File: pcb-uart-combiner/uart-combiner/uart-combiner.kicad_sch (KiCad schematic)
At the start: 26 parts, among them J1 Conn_01x03, J5 DBG UART, J6 SWD, J7 Conn_01x03, J8 Conn_01x03, J9 Conn_01x03

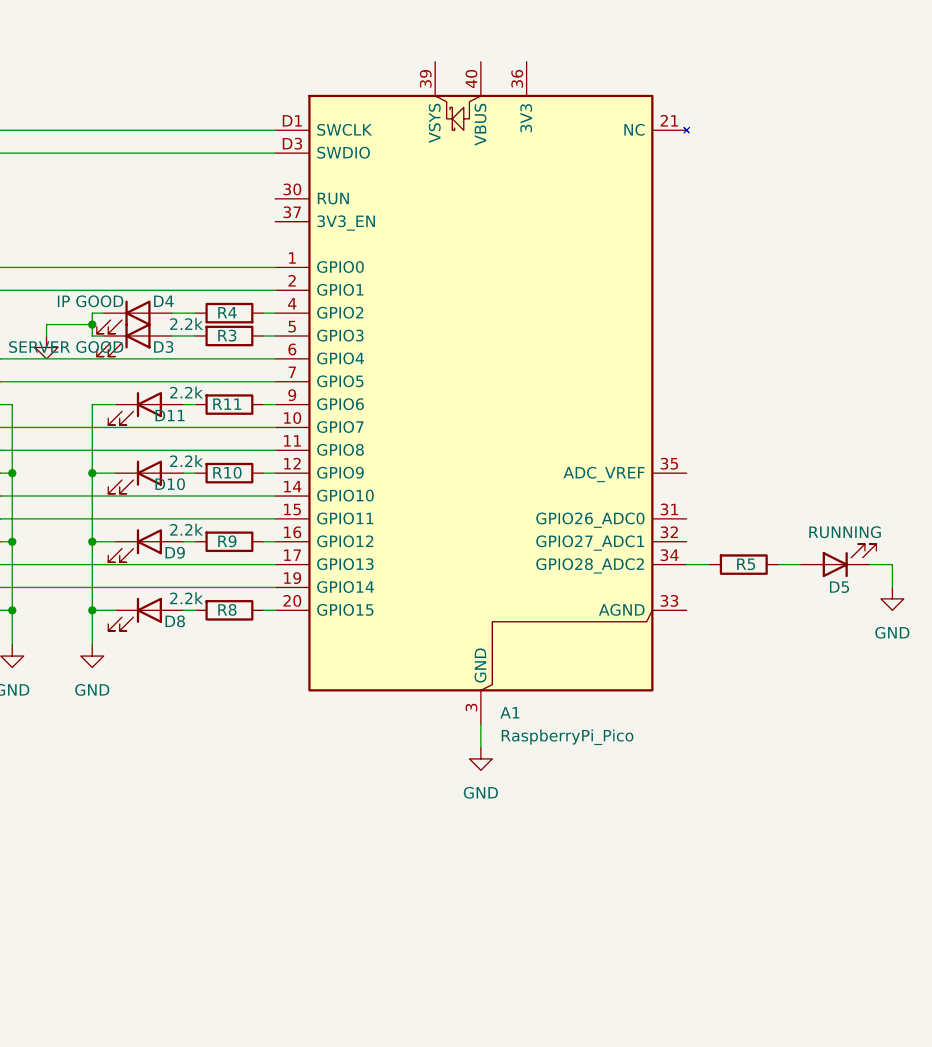
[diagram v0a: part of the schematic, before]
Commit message: Adjusting board size.
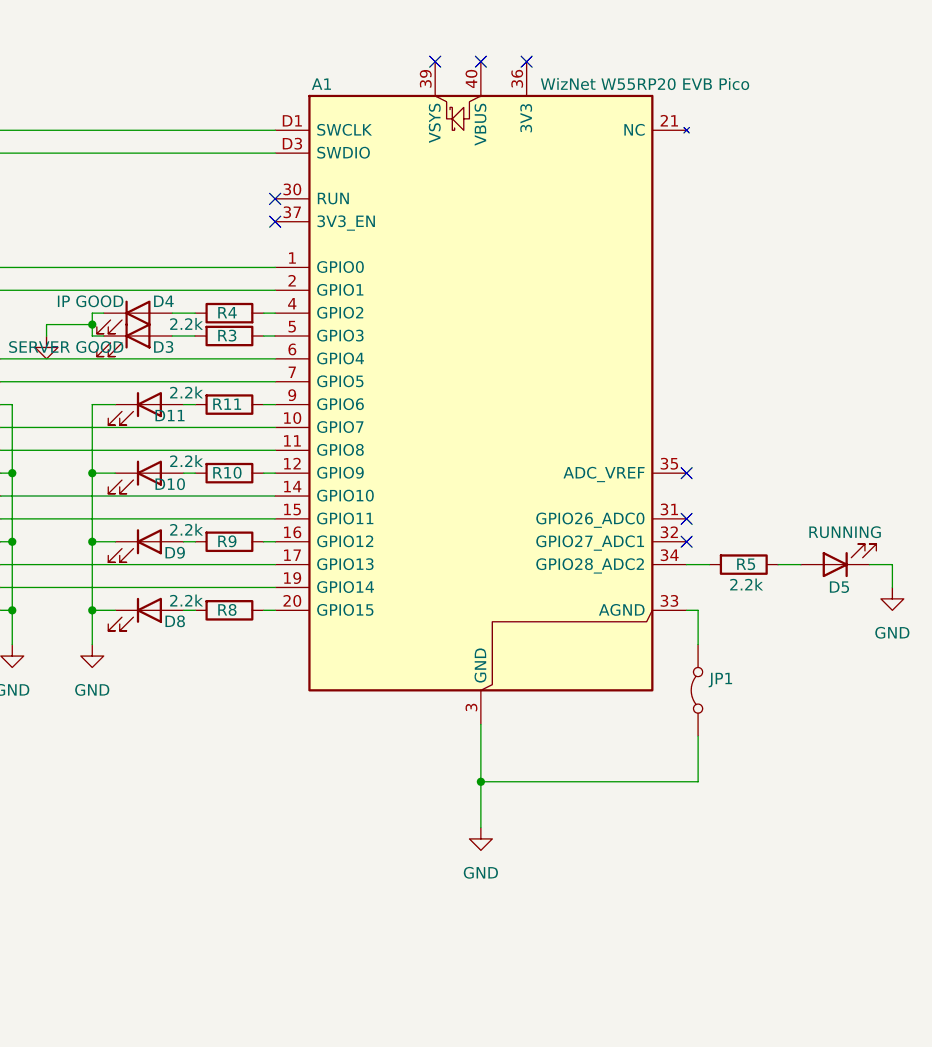
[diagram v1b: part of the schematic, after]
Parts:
- added JP1: Jumper_2_Bridged, Jumper:SolderJumper-2_P1.3mm_Bridged_RoundedPad1.0x1.5mm, symbol Jumper:Jumper_2_Bridged
- A1: value RaspberryPi_Pico -> WizNet W55RP20 EVB Pico
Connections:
- net GND: now also JP1.1 (A)
- net at A1.33 (AGND): now also JP1.2 (B)
- no-connect marks 0 -> 8
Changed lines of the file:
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@@
 	)
 	(junction
+		(at 114.3 130.81)
+		(diameter 0)
+		(color 0 0 0 0)
+	)
+	(junction
 		(at 71.12 80.01)
 		(diameter 0)
@@
 		(color 0 0 0 0)
 	)
+	(no_connect
+		(at 114.3 50.8)
+	)
+	(no_connect
+		(at 119.38 50.8)
+	)
+	(no_connect
+		(at 109.22 50.8)
+	)
+	(no_connect
+		(at 137.16 101.6)
+	)
+	(no_connect
+		(at 137.16 104.14)
+	)
+	(no_connect
+		(at 137.16 96.52)
+	)
+	(no_connect
+		(at 91.44 66.04)
+	)
+	(no_connect
+		(at 91.44 68.58)
+	)
 	(wire
 		(pts
@@
 	(wire
 		(pts
-			(xy 114.3 124.46) (xy 114.3 127)
+			(xy 114.3 124.46) (xy 114.3 130.81)
 		)
 		(stroke
@@
 	(wire
 		(pts
+			(xy 138.43 111.76) (xy 138.43 115.57)
+		)
+		(stroke
+			(width 0)
+			(type default)
+		)
+	)
+	(wire
+		(pts
 			(xy 90.17 78.74) (xy 91.44 78.74)
 		)
@@
 	(wire
 		(pts
+			(xy 138.43 130.81) (xy 114.3 130.81)
+		)
+		(stroke
+			(width 0)
+			(type default)
+		)
+	)
+	(wire
+		(pts
 			(xy 60.96 111.76) (xy 62.23 111.76)
 		)
@@
 	(wire
 		(pts
+			(xy 138.43 125.73) (xy 138.43 130.81)
+		)
+		(stroke
+			(width 0)
+			(type default)
+		)
+	)
+	(wire
+		(pts
 			(xy 60.96 109.22) (xy 91.44 109.22)
 		)
@@
 	(wire
 		(pts
+			(xy 114.3 130.81) (xy 114.3 135.89)
+		)
+		(stroke
+			(width 0)
+			(type default)
+		)
+	)
+	(wire
+		(pts
 			(xy 60.96 104.14) (xy 62.23 104.14)
 		)
@@
 	(wire
 		(pts
+			(xy 137.16 111.76) (xy 138.43 111.76)
+		)
+		(stroke
+			(width 0)
+			(type default)
+		)
+	)
+	(wire
+		(pts
 			(xy 53.34 68.58) (xy 53.34 77.47)
 		)
@@
 	(symbol
 		(lib_id "power:GND")
-		(at 114.3 127 0)
+		(at 114.3 135.89 0)
 		(unit 1)
 		(body_style 1)
@@
 		(fields_autoplaced yes)
 		(property "Reference" "#PWR05"
-			(at 114.3 133.35 0)
+			(at 114.3 142.24 0)
 			(hide yes)
 			(show_name no)
@@
 		)
 		(property "Value" "GND"
-			(at 114.3 132.08 0)
+			(at 114.3 140.97 0)
 			(show_name no)
 			(do_not_autoplace no)
@@
 		)
 		(property "Footprint" ""
-			(at 114.3 127 0)
+			(at 114.3 135.89 0)
 			(hide yes)
 			(show_name no)
@@
 		)
 		(property "Datasheet" ""
-			(at 114.3 127 0)
+			(at 114.3 135.89 0)
 			(hide yes)
 			(show_name no)
@@
 		)
 		(property "Description" "Power symbol creates a global label with name \"GND\" , ground"
-			(at 114.3 127 0)
+			(at 114.3 135.89 0)
 			(hide yes)
 			(show_name no)
@@
 	)
 	(symbol
+		(lib_id "Jumper:Jumper_2_Bridged")
+		(at 138.43 120.65 90)
+		(unit 1)
+		(body_style 1)
+		(exclude_from_sim no)
+		(in_bom yes)
+		(on_board yes)
+		(in_pos_files yes)
+		(dnp no)
+		(fields_autoplaced yes)
+		(property "Reference" "JP1"
+			(at 139.7 119.3799 90)
+			(show_name no)
+			(do_not_autoplace no)
+			(effects
+				(font
+					(size 1.27 1.27)
+				)
+				(justify right)
+			)
+		)
+		(property "Value" "Jumper_2_Bridged"
+			(at 139.7 121.9199 90)
+			(hide yes)
+			(show_name no)
+			(do_not_autoplace no)
+			(effects
+				(font
+					(size 1.27 1.27)
+				)
+				(justify right)
+			)
+		)
+		(property "Footprint" "Jumper:SolderJumper-2_P1.3mm_Bridged_RoundedPad1.0x1.5mm"
+			(at 138.43 120.65 0)
+			(hide yes)
+			(show_name no)
+			(do_not_autoplace no)
+			(effects
+				(font
+					(size 1.27 1.27)
+				)
+			)
+		)
+		(property "Datasheet" ""
+			(at 143.51 120.65 0)
+			(hide yes)
+			(show_name no)
+			(do_not_autoplace no)
+			(effects
+				(font
+					(size 1.27 1.27)
+				)
+			)
+		)
+		(property "Description" "Jumper, 2-pole, closed/bridged"
+			(at 146.05 120.65 0)
+			(hide yes)
+			(show_name no)
+			(do_not_autoplace no)
+			(effects
+				(font
+					(size 1.27 1.27)
+				)
+			)
+		)
+		(pin "1"
+		)
+		(pin "2"
+		)
+		(instances
+			(project "uart-combiner"
+				(path "/7f25198e-49d0-435a-a5a4-97946e7fb4eb"
+					(reference "JP1")
+					(unit 1)
+				)
+			)
+		)
+	)
+	(symbol
 		(lib_id "Device:R")
 		(at 86.36 88.9 270)
@@
 		)
 		(property "Value" "2.2k"
-			(at 143.51 110.49 90)
-			(hide yes)
+			(at 143.764 108.966 90)
 			(show_name no)
 			(do_not_autoplace no)
@@
 		)
 		(property "Value" "2.2k"
-			(at 81.534 110.49 90)
+			(at 81.534 110.744 90)
 			(show_name no)
 			(do_not_autoplace no)
@@
 		(in_pos_files yes)
 		(dnp no)
-		(fields_autoplaced yes)
 		(property "Reference" "A1"
-			(at 116.4433 123.19 0)
+			(at 95.504 53.34 0)
 			(show_name no)
 			(do_not_autoplace no)
@@
 			)
 		)
-		(property "Value" "RaspberryPi_Pico"
-			(at 116.4433 125.73 0)
+		(property "Value" "WizNet W55RP20 EVB Pico"
+			(at 120.904 53.34 0)
 			(show_name no)
 			(do_not_autoplace no)

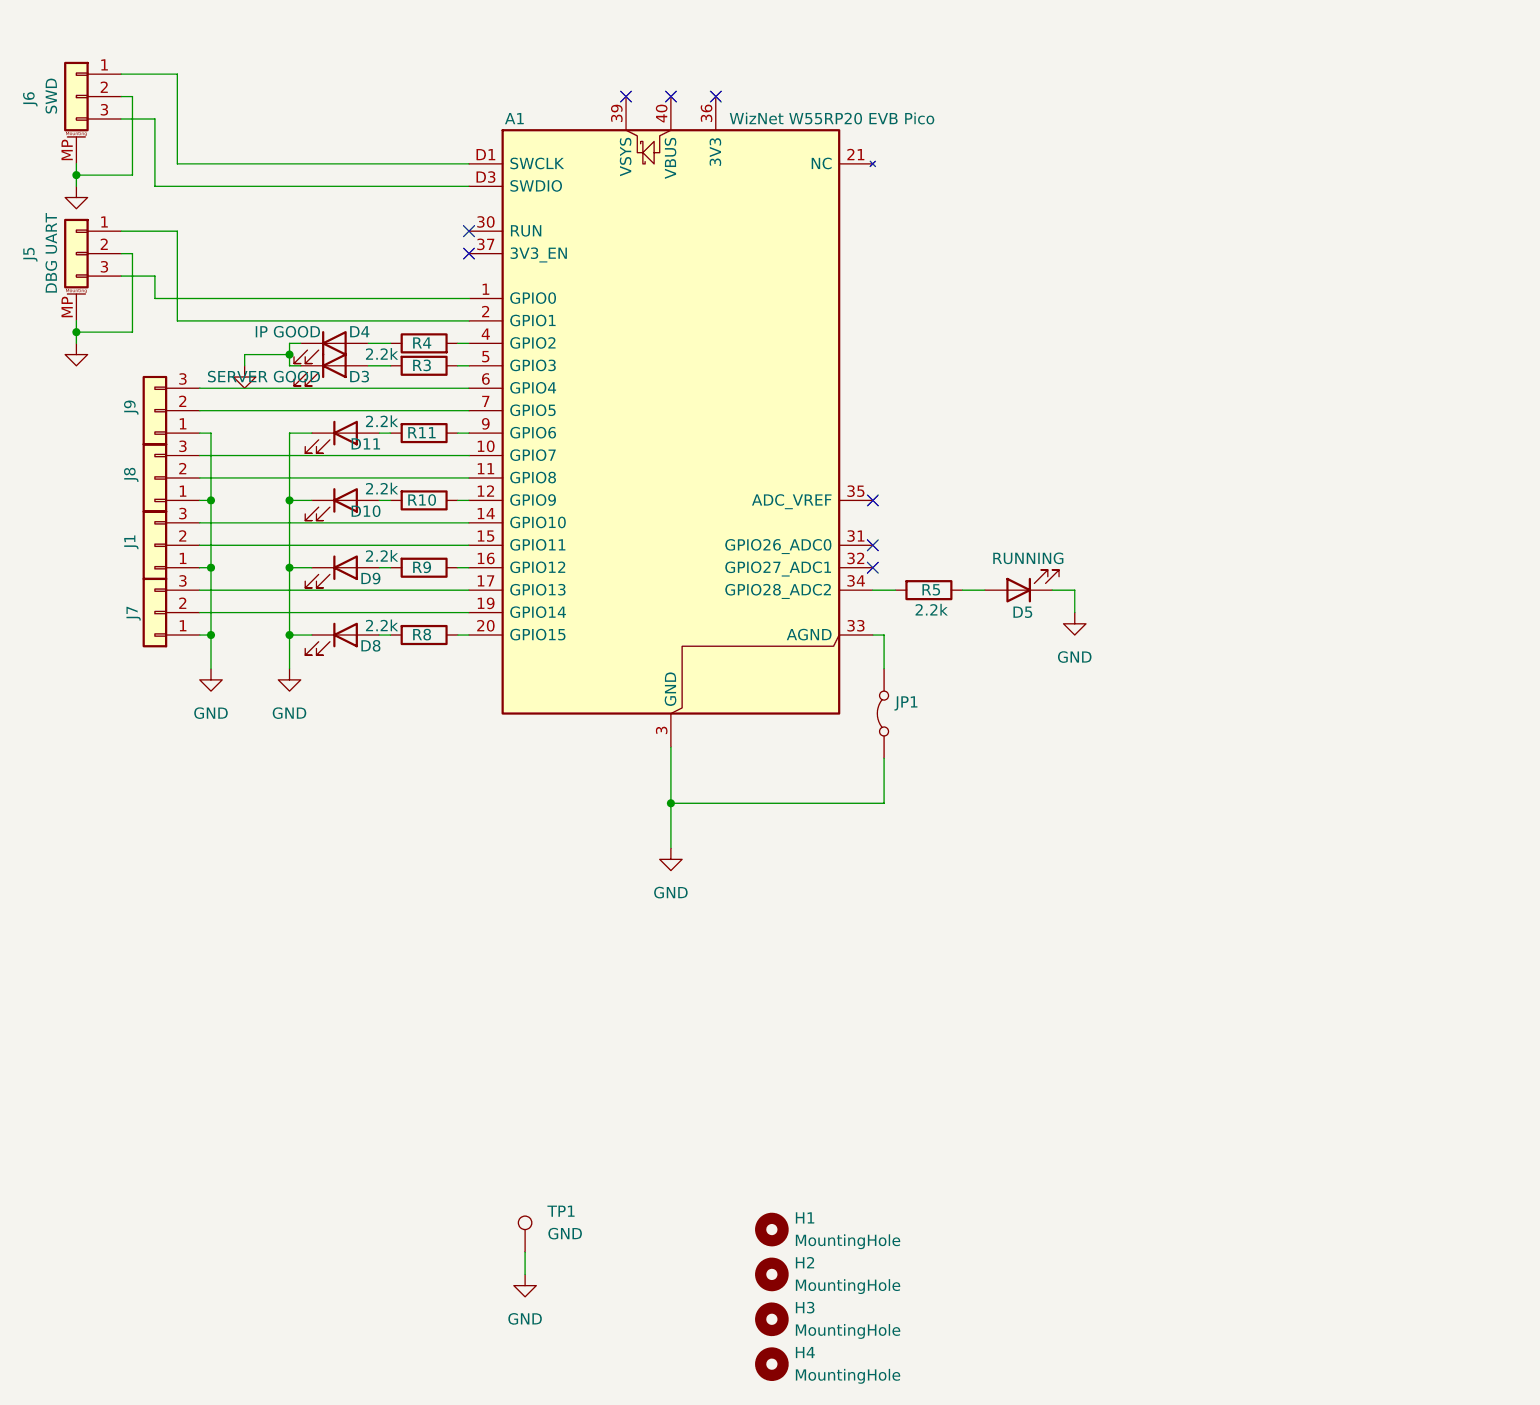
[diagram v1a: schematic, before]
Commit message: Replacing 3pin connectors with 4pin ones.
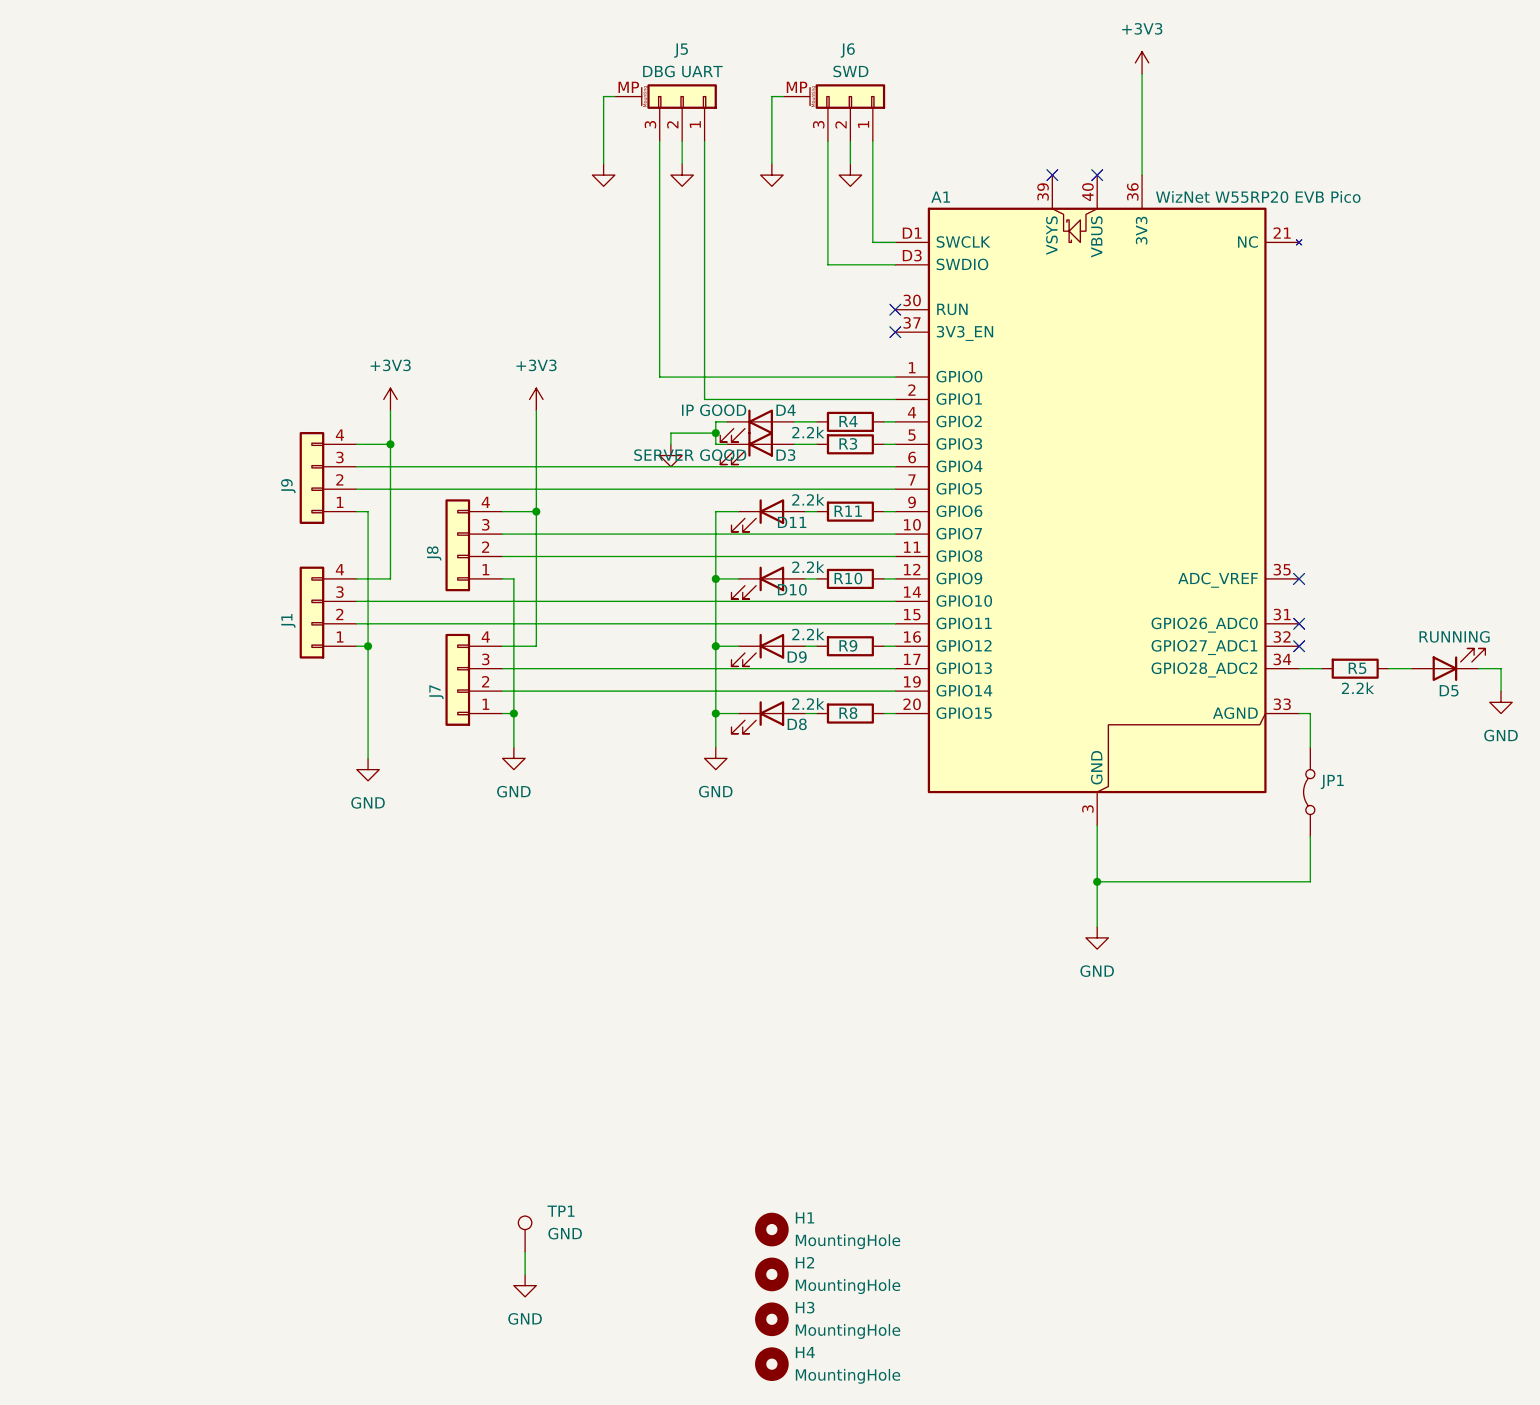
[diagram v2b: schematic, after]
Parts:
- J1, J7, J8, J9: footprint Connector_JST:JST_PH_B3B-PH-K_1x03_P2.00mm_Vertical -> Connector_JST:JST_PH_B4B-PH-K_1x04_P2.00mm_Vertical; symbol Connector_Generic:Conn_01x03 -> Connector_Generic:Conn_01x04
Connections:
- net +3V3: now reaches A1.36 (3V3)
- net +3V3: now also J1.4 (Pin_4), J7.4 (Pin_4), J8.4 (Pin_4), J9.4 (Pin_4)
- no-connect marks 8 -> 7
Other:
- moved on the sheet: A1, D10, D11, D3, D4, D5, D8, D9, J5, J6, JP1, R10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

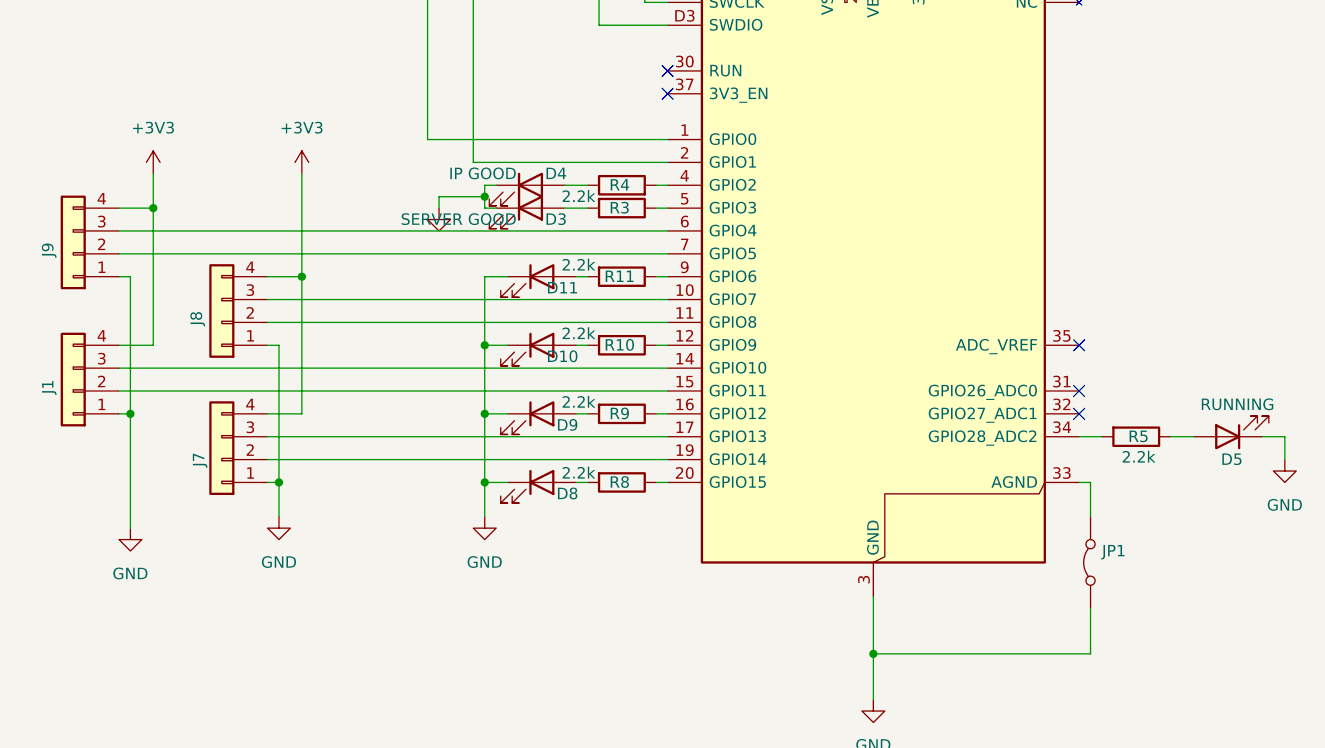
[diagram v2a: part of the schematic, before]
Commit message: Fine tuning UART combiner.
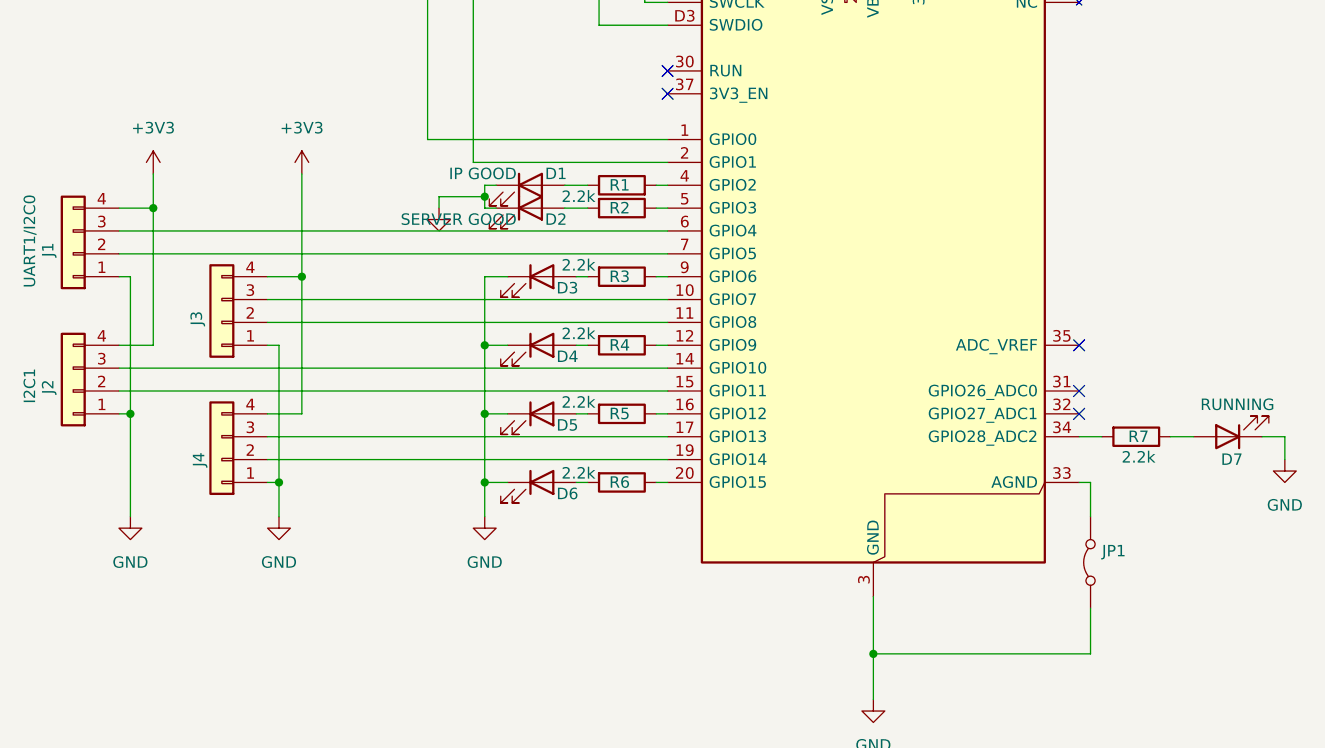
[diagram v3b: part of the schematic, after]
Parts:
- J1: renamed from J9; value Conn_01x03 -> UART1/I2C0
- J2: renamed from J1; value Conn_01x03 -> I2C1
- renumbered D4 to D1, D3 to D2, D11 to D3, D10 to D4, D9 to D5, D8 to D6, D5 to D7, J8 to J3, J7 to J4, R4 to R1, R3 to R2, R11 to R3, R10 to R4, R9 to R5, R8 to R6, R5 to R7
